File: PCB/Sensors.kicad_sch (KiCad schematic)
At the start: 14 parts, among them U301 MMC5633NJL, U302 LSM6DSV320, U303 MS5607-02BA, U304 SAM-M8Q

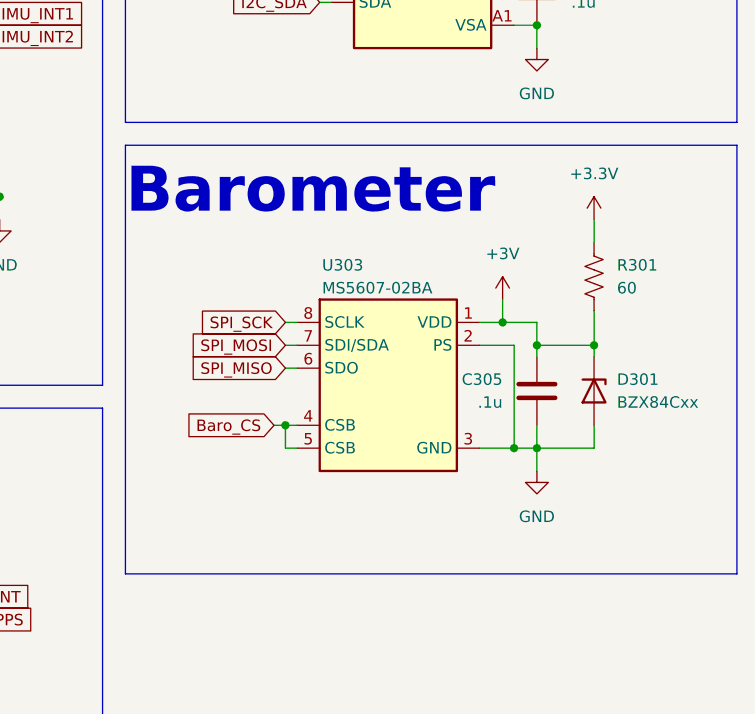
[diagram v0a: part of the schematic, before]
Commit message: Created Bill of materials for the computer
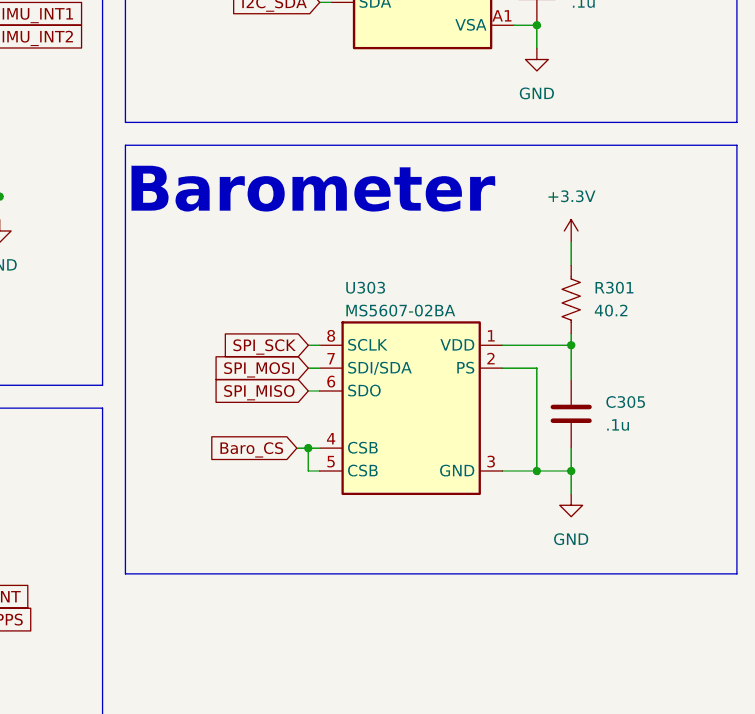
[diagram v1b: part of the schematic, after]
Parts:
- removed D301: BZX84Cxx, Package_TO_SOT_SMD:SOT-23_Handsoldering, symbol Diode:BZX84Cxx
- R301: value 60 -> 40.2
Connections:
- net +3V: no longer names the net of C305.1, R301.2, U303.1 (VDD)
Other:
- moved on the sheet: C305, R301, U303

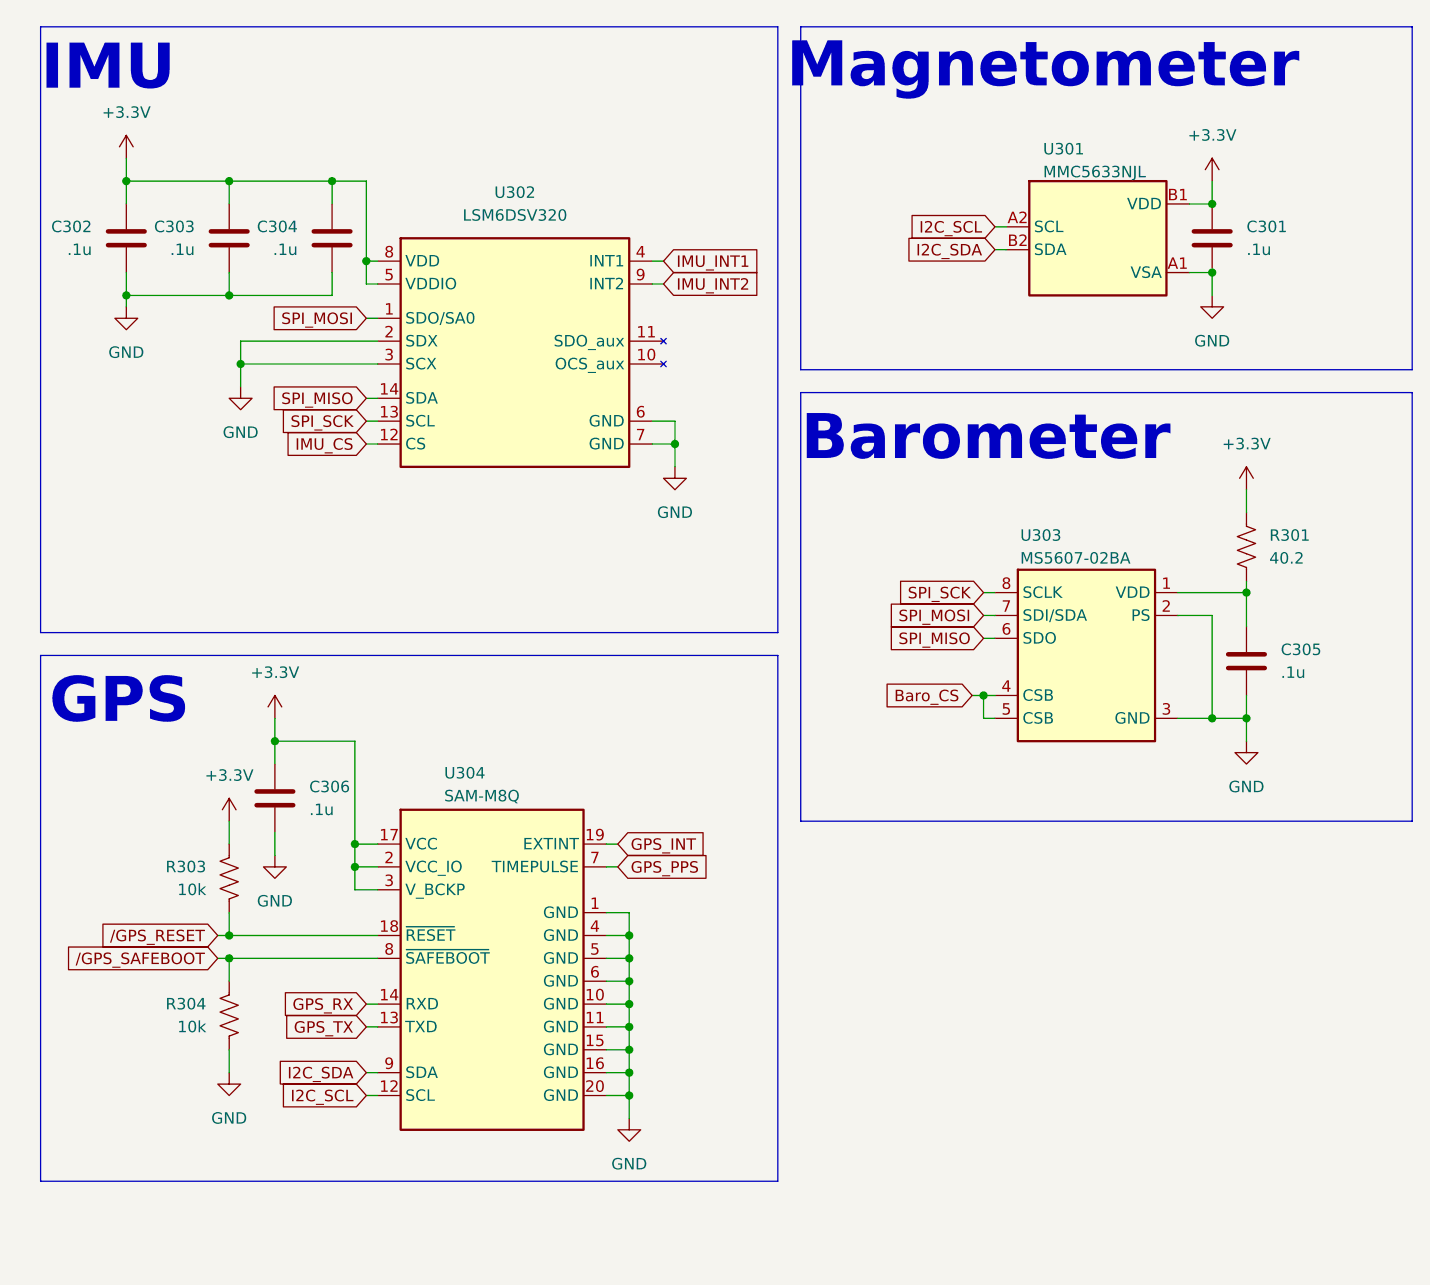
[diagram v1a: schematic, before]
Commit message: Cleaned up the schematic and replace and rerouted everything, also replace radio with a module
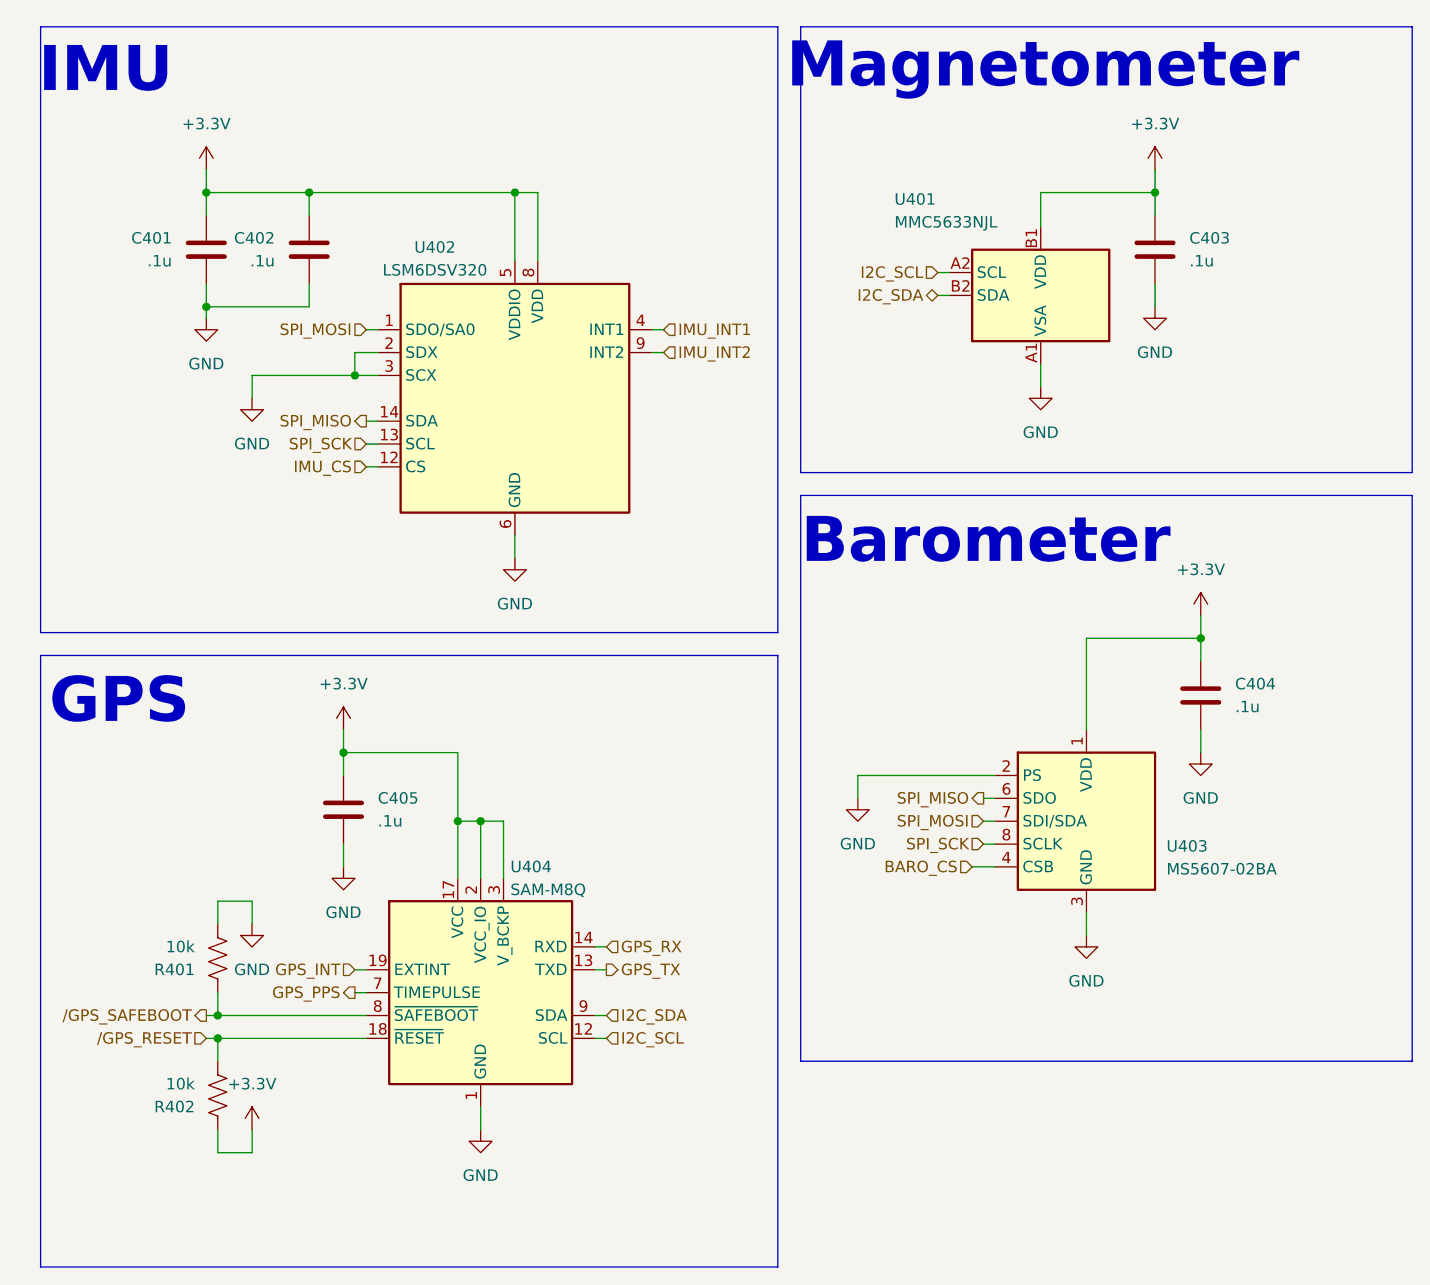
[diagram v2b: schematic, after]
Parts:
- removed C304: .1u, Capacitor_SMD:C_0603_1608Metric_Pad1.08x0.95mm_HandSolder, symbol Device:C
- removed R301: 40.2, Resistor_SMD:R_0603_1608Metric_Pad0.98x0.95mm_HandSolder, symbol Device:R_US
- U404: renamed from U304; footprint RF_GPS:ublox_SAM-M8Q_HandSolder -> RF_GPS:ublox_SAM-M8Q
- renumbered C302 to C401, C303 to C402, C301 to C403, C305 to C404, C306 to C405, R304 to R401, R303 to R402, U301 to U401, U302 to U402, U303 to U403
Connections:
- net +3.3V: now also C404.1, U403.1 (VDD)
- net Baro_CS renamed BARO_CS
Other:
- moved on the sheet: C401, C402, C403, C404, C405, R401, R402, U401

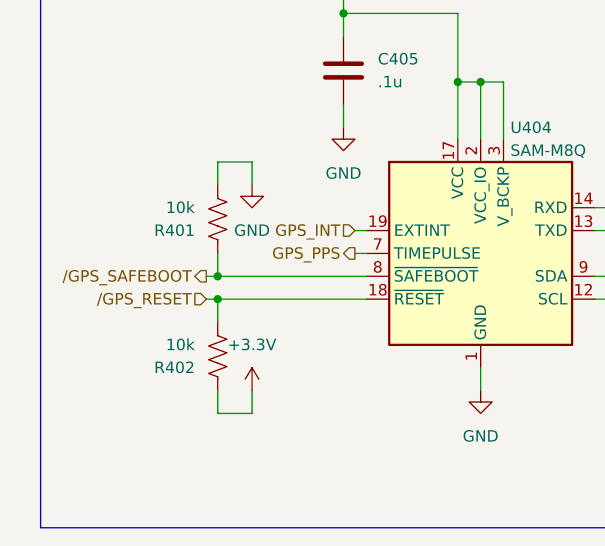
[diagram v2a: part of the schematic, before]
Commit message: - Updated schematic with solutions to the hardware problems - Remove files that are the .gitignore
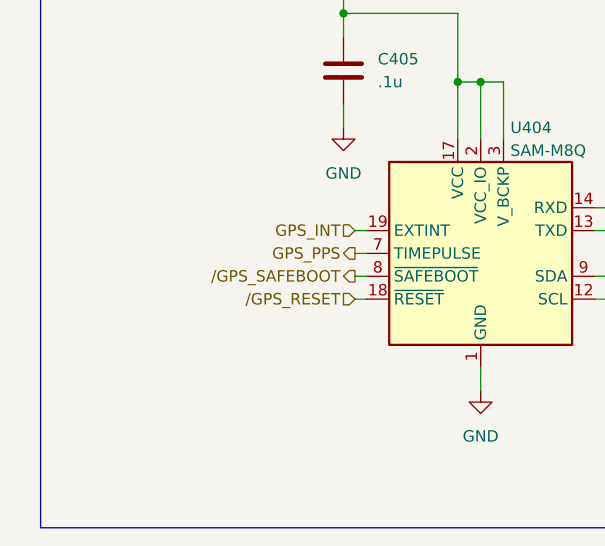
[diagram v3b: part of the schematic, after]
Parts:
- removed R401, R402: 10k, Resistor_SMD:R_0603_1608Metric_Pad0.98x0.95mm_HandSolder, symbol Device:R_US

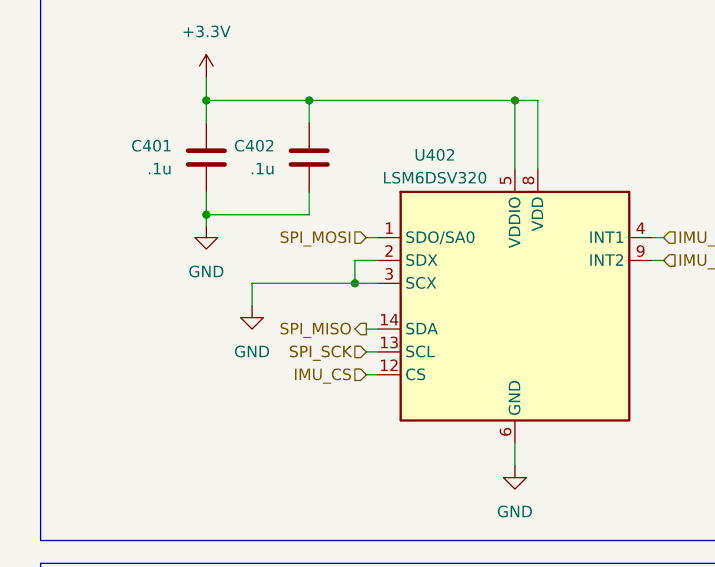
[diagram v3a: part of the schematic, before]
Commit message: Switched MISO and MOSI for IMU, fixed some DRC Errors
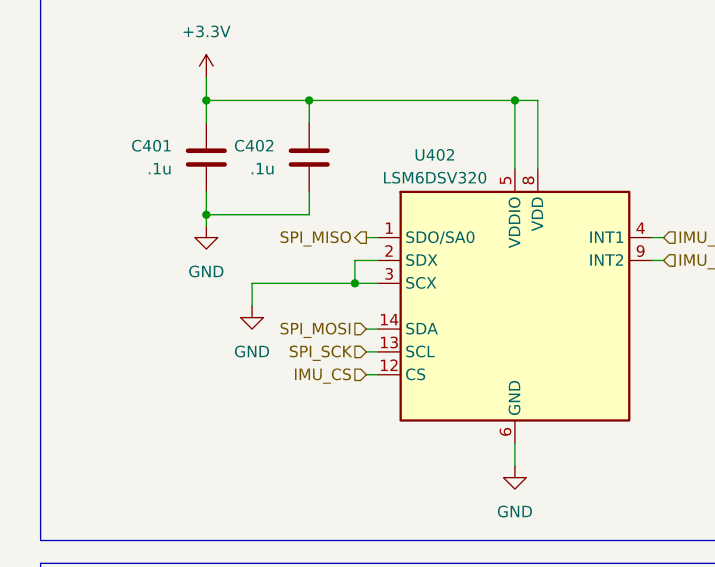
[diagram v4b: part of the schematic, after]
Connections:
- net SPI_MISO: now also U402.1 (SDO/SA0); no longer U402.14 (SDA)
- net SPI_MOSI: now also U402.14 (SDA); no longer U402.1 (SDO/SA0)
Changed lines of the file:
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@@
+	(wire
+		(pts
+			(xy 133.35 85.09) (xy 146.05 85.09)
+		)
+		(stroke
+			(width 0)
+			(type default)
+		)
+	)
+	(wire
+		(pts
+			(xy 116.84 44.45) (xy 118.11 44.45)
+		)
+		(stroke
+			(width 0)
+			(type default)
+		)
+	)
+	(wire
+		(pts
+			(xy 40.64 58.42) (xy 40.64 55.88)
+		)
+		(stroke
+			(width 0)
+			(type default)
+		)
+	)
+	(wire
+		(pts
+			(xy 35.56 35.56) (xy 46.99 35.56)
+		)
+		(stroke
+			(width 0)
+			(type default)
+		)
+	)
+	(wire
+		(pts
+			(xy 46.99 35.56) (xy 46.99 38.1)
+		)
+		(stroke
+			(width 0)
+			(type default)
+		)
+	)
+	(wire
+		(pts
+			(xy 121.92 105.41) (xy 123.19 105.41)
+		)
+		(stroke
+			(width 0)
+			(type default)
+		)
+	)
+	(wire
+		(pts
+			(xy 53.34 66.04) (xy 54.61 66.04)
+		)
+		(stroke
+			(width 0)
+			(type default)
+		)
+	)
+	(wire
+		(pts
+			(xy 128.27 54.61) (xy 128.27 57.15)
+		)
+		(stroke
+			(width 0)
+			(type default)
+		)
+	)
+	(wire
+		(pts
+			(xy 50.8 97.79) (xy 50.8 100.33)
+		)
+		(stroke
+			(width 0)
+			(type default)
+		)
+	)
+	(wire
+		(pts
+			(xy 63.5 105.41) (xy 63.5 111.76)
+		)
+		(stroke
+			(width 0)
+			(type default)
+		)
+	)
 	(wire
 		(pts
@@
 	(wire
 		(pts
-			(xy 133.35 85.09) (xy 146.05 85.09)
-		)
-		(stroke
-			(width 0)
-			(type default)
-		)
-	)
-	(wire
-		(pts
-			(xy 116.84 44.45) (xy 118.11 44.45)
-		)
-		(stroke
-			(width 0)
-			(type default)
-		)
-	)
-	(wire
-		(pts
-			(xy 40.64 58.42) (xy 40.64 55.88)
-		)
-		(stroke
-			(width 0)
-			(type default)
-		)
-	)
-	(wire
-		(pts
-			(xy 35.56 35.56) (xy 46.99 35.56)
-		)
-		(stroke
-			(width 0)
-			(type default)
-		)
-	)
-	(wire
-		(pts
-			(xy 46.99 35.56) (xy 46.99 38.1)
-		)
-		(stroke
-			(width 0)
-			(type default)
-		)
-	)
-	(wire
-		(pts
-			(xy 121.92 105.41) (xy 123.19 105.41)
-		)
-		(stroke
-			(width 0)
-			(type default)
-		)
-	)
-	(wire
-		(pts
-			(xy 53.34 66.04) (xy 54.61 66.04)
-		)
-		(stroke
-			(width 0)
-			(type default)
-		)
-	)
-	(wire
-		(pts
-			(xy 128.27 54.61) (xy 128.27 57.15)
-		)
-		(stroke
-			(width 0)
-			(type default)
-		)
-	)
-	(wire
-		(pts
-			(xy 50.8 97.79) (xy 50.8 100.33)
-		)
-		(stroke
-			(width 0)
-			(type default)
-		)
-	)
-	(wire
-		(pts
-			(xy 63.5 105.41) (xy 63.5 111.76)
-		)
-		(stroke
-			(width 0)
-			(type default)
-		)
-	)
-	(wire
-		(pts
 			(xy 107.95 102.87) (xy 107.95 100.33)
 		)
@@
 	(wire
 		(pts
+			(xy 146.05 85.09) (xy 146.05 87.63)
+		)
+		(stroke
+			(width 0)
+			(type default)
+		)
+	)
+	(wire
+		(pts
+			(xy 128.27 35.56) (xy 140.97 35.56)
+		)
+		(stroke
+			(width 0)
+			(type default)
+		)
+	)
+	(wire
+		(pts
+			(xy 46.99 35.56) (xy 69.85 35.56)
+		)
+		(stroke
+			(width 0)
+			(type default)
+		)
+	)
+	(wire
+		(pts
+			(xy 54.61 55.88) (xy 52.07 55.88)
+		)
+		(stroke
+			(width 0)
+			(type default)
+		)
+	)
+	(wire
+		(pts
+			(xy 146.05 95.25) (xy 146.05 97.79)
+		)
+		(stroke
+			(width 0)
+			(type default)
+		)
+	)
+	(wire
+		(pts
 			(xy 53.34 60.96) (xy 54.61 60.96)
 		)
@@
 	(wire
 		(pts
-			(xy 146.05 85.09) (xy 146.05 87.63)
-		)
-		(stroke
-			(width 0)
-			(type default)
-		)
-	)
-	(wire
-		(pts
-			(xy 128.27 35.56) (xy 140.97 35.56)
-		)
-		(stroke
-			(width 0)
-			(type default)
-		)
-	)
-	(wire
-		(pts
-			(xy 46.99 35.56) (xy 69.85 35.56)
-		)
-		(stroke
-			(width 0)
-			(type default)
-		)
-	)
-	(wire
-		(pts
-			(xy 54.61 55.88) (xy 52.07 55.88)
-		)
-		(stroke
-			(width 0)
-			(type default)
-		)
-	)
-	(wire
-		(pts
-			(xy 146.05 95.25) (xy 146.05 97.79)
-		)
-		(stroke
-			(width 0)
-			(type default)
-		)
-	)
-	(wire
-		(pts
 			(xy 52.07 127) (xy 53.34 127)
 		)
@@
 	(hierarchical_label "SPI_MOSI"
 		(shape input)
-		(at 53.34 50.8 180)
+		(at 53.34 60.96 180)
 		(effects
 			(font
@@
 	(hierarchical_label "SPI_MISO"
 		(shape output)
-		(at 53.34 60.96 180)
-		(effects
-			(font
+		(at 53.34 50.8 180)
+		(effects
+			(font
